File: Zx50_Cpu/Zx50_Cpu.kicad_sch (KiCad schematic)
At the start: 18 parts

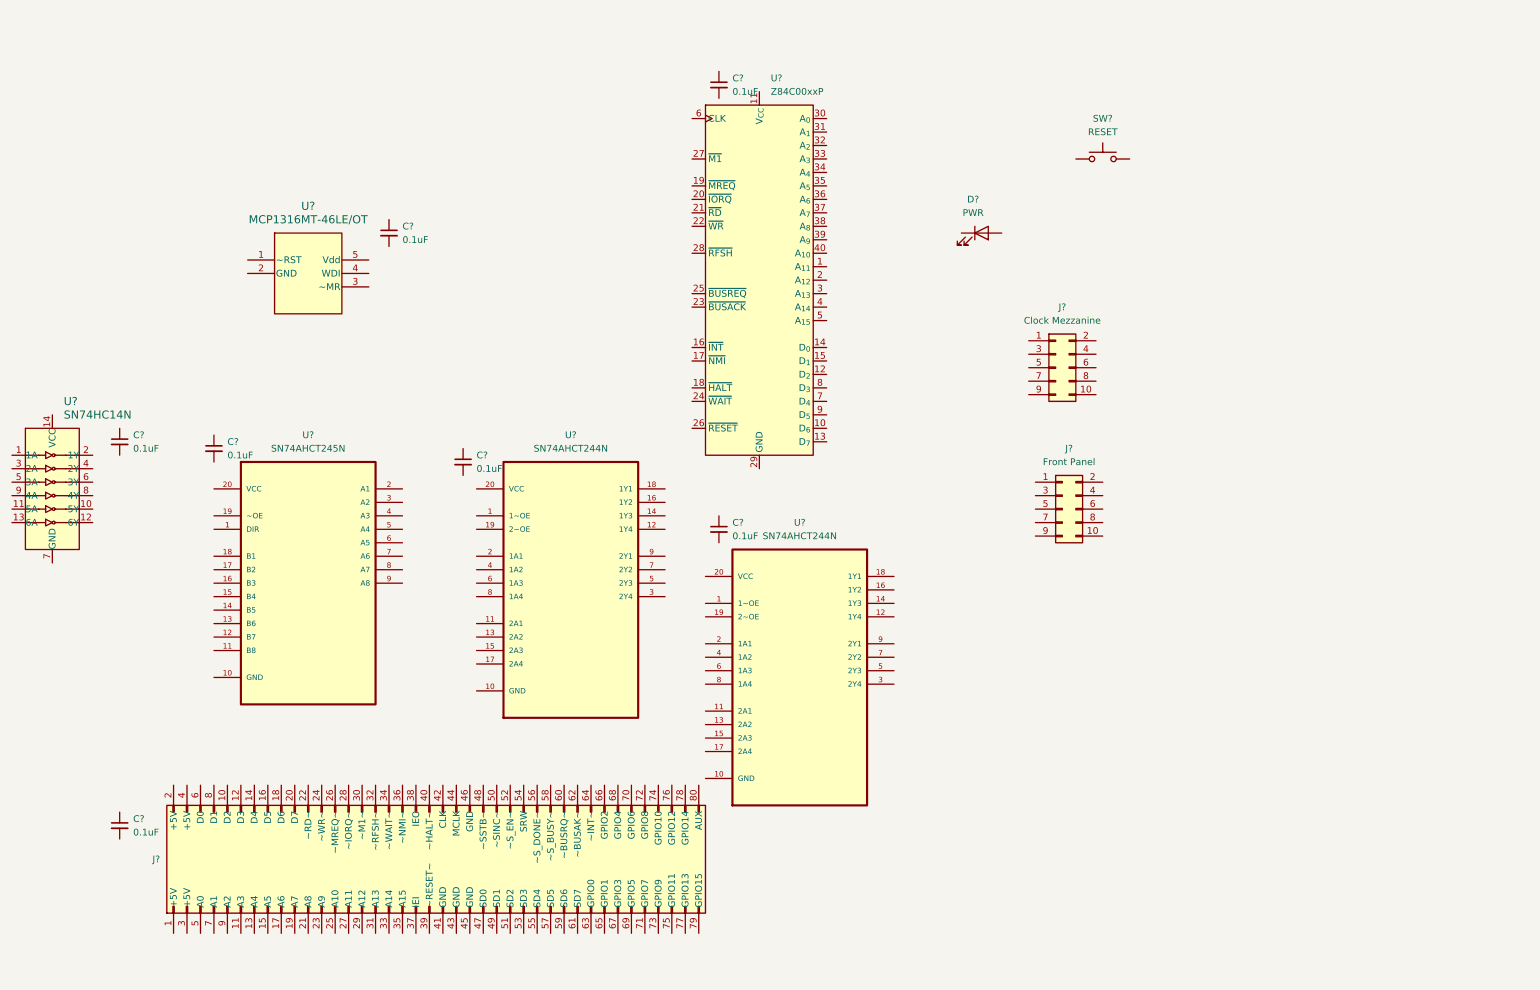
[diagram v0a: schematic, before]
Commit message: final cpu schematic before pcb layout
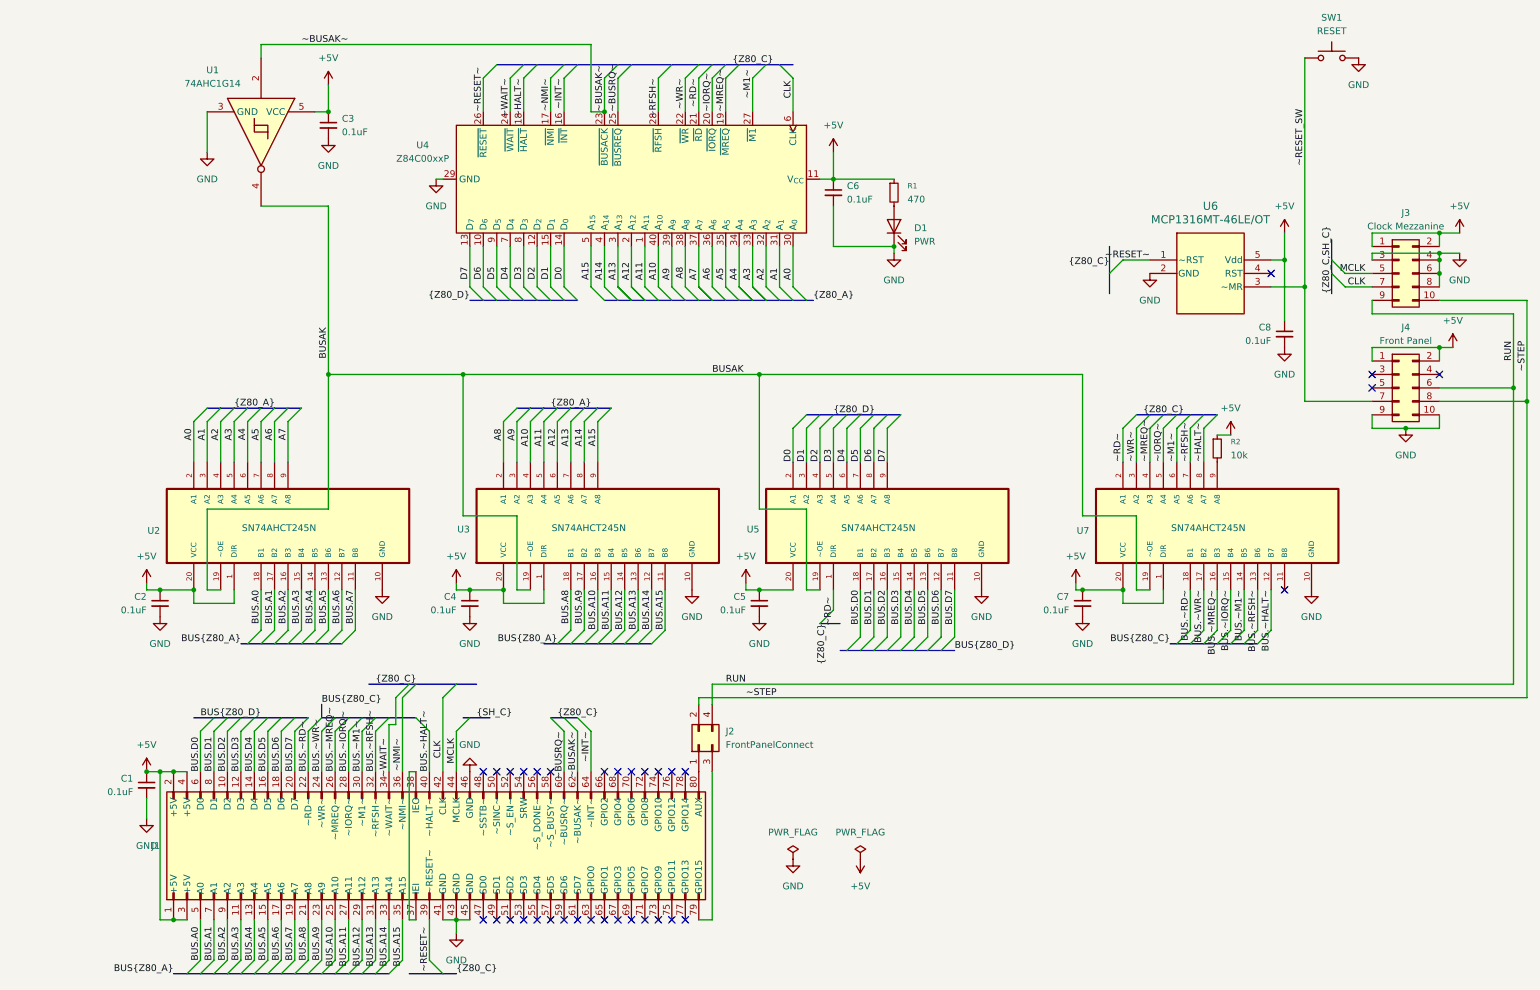
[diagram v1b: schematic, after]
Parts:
- removed C? (x4): 0.1uF, symbol zx50_symbols:C_0_1uF
- removed J?: Zx50_EdgeConnector, Connector_PinSocket_2.54mm:PinSocket_2x40_P2.54mm_Vertical_Oval, symbol zx50_symbols:Zx50_EdgeConnector
- removed U? (x2): SN74AHCT244N, Package_DIP:DIP-20_W7.62mm_Socket, symbol zx50_symbols:74AHCT244
- removed U?: SN74HC14N, digikey-footprints:DIP-14_W3mm, symbol dk_Logic-Gates-and-Inverters:SN74HC14N
- added C2, C3, C4, C7, C8: 0.1uF, Capacitor_THT:C_Disc_D5.0mm_W2.5mm_P5.00mm, symbol zx50_symbols:C_0_1uF
- added J1: Zx50_EdgeConnector, Connector_PinSocket_2.54mm:PinSocket_2x40_P2.54mm_Vertical_Oval, symbol zx50_symbols:Zx50_EdgeConnector
- added J2: FrontPanelConnect, Connector_PinSocket_2.54mm:PinSocket_2x02_P2.54mm_Vertical, symbol Connector_Generic:Conn_02x02_Odd_Even
- added R1: 470, Resistor_THT:R_Axial_DIN0207_L6.3mm_D2.5mm_P10.16mm_Horizontal, symbol Device:R_Small
- added R2: 10k, Resistor_THT:R_Axial_DIN0207_L6.3mm_D2.5mm_P10.16mm_Horizontal, symbol Device:R_Small
- added U1: 74AHC1G14, Package_TO_SOT_SMD:SOT-23-5_HandSoldering, symbol zx50_symbols:74AHC1G14
- added U2, U3, U7: SN74AHCT245N, Package_DIP:DIP-20_W7.62mm_Socket, symbol zx50_symbols:74AHCT245
- C1, C5, C6: renamed from C?; footprint (none) -> Capacitor_THT:C_Disc_D5.0mm_W2.5mm_P5.00mm; DigiKey_PN (none) -> BC1101CT-ND
- U5: renamed from U?; symbol zx50_symbols:SN74AHCT245N -> zx50_symbols:74AHCT245
- U6: renamed from U?; symbol zx50_symbols:MCP1316MT-46LE_OT -> zx50_symbols:MCP1318MT-46LE_OT; Digikey_PN MCP1316MT-46LE/OTCT-ND -> MCP1318MT-46LE/OTCT-ND
- gave numbers to parts that had none: 5
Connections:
- net ~RESET_SW: now reaches SW1.1
- net ~RESET_SW: now also J4.7 (Pin_7), U6.3 (~MR)
- net GND: now reaches SW1.2
- net GND: now also C1.2, C5.2, C6.2, D1.1 (K), J3.3 (Pin_3), J3.4 (Pin_4), J3.6 (Pin_6), J3.8 (Pin_8), J4.10 (Pin_10), J4.9 (Pin_9), U4.29 (GND), U5.10 (GND), U6.2 (GND), C2.2, C3.2, C4.2, C7.2, C8.2, J1.41 (GND), J1.43 (GND), J1.45 (GND), J1.46 (GND), U1.3 (GND), U2.10 (GND), U3.10 (GND), U7.10 (GND)
- net +5V: now reaches C5.1
- net +5V: now also C1.1, C6.1, J3.1 (Pin_1), J3.2 (Pin_2), J4.1 (Pin_1), J4.2 (Pin_2), U4.11 (V_{CC}), U5.20 (VCC), U6.5 (Vdd), C2.1, C3.1, C4.1, C7.1, C8.1, J1.1 (+5V), J1.2 (+5V), J1.3 (+5V), J1.4 (+5V), R1.1, R2.1, U1.5 (VCC), U2.1 (DIR), U2.20 (VCC), U3.1 (DIR), U3.20 (VCC), U7.1 (DIR), U7.20 (VCC)
- net ~RESET~: now reaches U6.1 (~RST)
- net ~RESET~: now also U4.26 (~{RESET}), J1.39 (~RESET~)
- net at D1.2 (A): now also R1.2
- net RUN: now reaches J4.6 (Pin_6)
- net RUN: now also J3.9 (Pin_9), J2.4 (Pin_4)
- net ~STEP: now reaches J4.8 (Pin_8)
- net ~STEP: now also J3.10 (Pin_10), J2.2 (Pin_2)
- net MCLK: now reaches J3.5 (Pin_5)
- net MCLK: now also J1.44 (MCLK)
- net CLK: now reaches J3.7 (Pin_7)
- net CLK: now also U4.6 (CLK), J1.42 (CLK)
- net A11: now reaches U4.1 (A_{11})
- net A11: now also U3.5 (A4)
- net D6: now reaches U4.10 (D_{6})
- net D6: now also U5.8 (A7)
- net D2: now reaches U4.12 (D_{2})
- net D2: now also U5.4 (A3)
- net D7: now reaches U4.13 (D_{7})
- net D7: now also U5.9 (A8)
- net D0: now reaches U4.14 (D_{0})
- net D0: now also U5.2 (A1)
- net D1: now reaches U4.15 (D_{1})
- net D1: now also U5.3 (A2)
- net ~INT~: now reaches U4.16 (~{INT})
- net ~INT~: now also J1.64 (~INT~)
- net ~NMI~: now reaches U4.17 (~{NMI})
- net ~NMI~: now also J1.36 (~NMI~)
- net ~HALT~: now reaches U4.18 (~{HALT})
- net ~HALT~: now also U7.8 (A7)
- net ~MREQ~: now reaches U4.19 (~{MREQ})
- net ~MREQ~: now also U7.4 (A3)
- net A12: now reaches U4.2 (A_{12})
- net A12: now also U3.6 (A5)
- net ~IORQ~: now reaches U4.20 (~{IORQ})
- net ~IORQ~: now also U7.5 (A4)
- net ~RD~: now reaches U4.21 (~{RD})
- net ~RD~: now also U5.1 (DIR), U7.2 (A1)
- net ~WR~: now reaches U4.22 (~{WR})
- net ~WR~: now also U7.3 (A2)
- net ~BUSAK~: now reaches U4.23 (~{BUSACK})
- net ~BUSAK~: now also J1.62 (~BUSAK~), U1.2
- net ~WAIT~: now reaches U4.24 (~{WAIT})
- net ~WAIT~: now also J1.34 (~WAIT~)
- net ~BUSRQ~: now reaches U4.25 (~{BUSREQ})
- net ~BUSRQ~: now also J1.60 (~BUSRQ~)
- net ~M1~: now reaches U4.27 (~{M1})
- net ~M1~: now also U7.6 (A5)
- net ~RFSH~: now reaches U4.28 (~{RFSH})
- net ~RFSH~: now also U7.7 (A6)
- net A13: now reaches U4.3 (A_{13})
- net A13: now also U3.7 (A6)
- net A0: now reaches U4.30 (A_{0})
- net A0: now also U2.2 (A1)
- net A1: now reaches U4.31 (A_{1})
- net A1: now also U2.3 (A2)
- net A2: now reaches U4.32 (A_{2})
- net A2: now also U2.4 (A3)
- net A3: now reaches U4.33 (A_{3})
- net A3: now also U2.5 (A4)
- net A4: now reaches U4.34 (A_{4})
- net A4: now also U2.6 (A5)
- net A5: now reaches U4.35 (A_{5})
- net A5: now also U2.7 (A6)
- net A6: now reaches U4.36 (A_{6})
- net A6: now also U2.8 (A7)
- net A7: now reaches U4.37 (A_{7})
- net A7: now also U2.9 (A8)
- net A8: now reaches U4.38 (A_{8})
- net A8: now also U3.2 (A1)
- net A9: now reaches U4.39 (A_{9})
- net A9: now also U3.3 (A2)
- net A14: now reaches U4.4 (A_{14})
- net A14: now also U3.8 (A7)
- net A10: now reaches U4.40 (A_{10})
- net A10: now also U3.4 (A3)
- net A15: now reaches U4.5 (A_{15})
- net A15: now also U3.9 (A8)
- net D4: now reaches U4.7 (D_{4})
- net D4: now also U5.6 (A5)
- net D3: now reaches U4.8 (D_{3})
- net D3: now also U5.5 (A4)
- net D5: now reaches U4.9 (D_{5})
- net D5: now also U5.7 (A6)
- net BUS.D7: now reaches U5.11 (B8)
- net BUS.D7: now also J1.20 (D7)
- net BUS.D6: now reaches U5.12 (B7)
- net BUS.D6: now also J1.18 (D6)
- net BUS.D5: now reaches U5.13 (B6)
- net BUS.D5: now also J1.16 (D5)
- net BUS.D4: now reaches U5.14 (B5)
- net BUS.D4: now also J1.14 (D4)
- net BUS.D3: now reaches U5.15 (B4)
- net BUS.D3: now also J1.12 (D3)
- net BUS.D2: now reaches U5.16 (B3)
- net BUS.D2: now also J1.10 (D2)
- net BUS.D1: now reaches U5.17 (B2)
- net BUS.D1: now also J1.8 (D1)
- net BUS.D0: now reaches U5.18 (B1)
- net BUS.D0: now also J1.6 (D0)
- net BUSAK: now reaches U5.19 (~OE)
- net BUSAK: now also U1.4, U2.19 (~OE), U3.19 (~OE), U7.19 (~OE)
- new net: R2.2, U7.9 (A8)
- new net: J1.37 (IEI), J1.38 (IEO)
- new net: J1.79 (GPIO15), J2.3 (Pin_3)
- new net: J1.80 (AUX), J2.1 (Pin_1)
- new net BUS.A0: J1.5 (A0), U2.18 (B1)
- new net BUS.A1: J1.7 (A1), U2.17 (B2)
- new net BUS.A10: J1.25 (A10), U3.16 (B3)
- new net BUS.A11: J1.27 (A11), U3.15 (B4)
- new net BUS.A12: J1.29 (A12), U3.14 (B5)
- new net BUS.A13: J1.31 (A13), U3.13 (B6)
- new net BUS.A14: J1.33 (A14), U3.12 (B7)
- new net BUS.A15: J1.35 (A15), U3.11 (B8)
- new net BUS.A2: J1.9 (A2), U2.16 (B3)
- new net BUS.A3: J1.11 (A3), U2.15 (B4)
- new net BUS.A4: J1.13 (A4), U2.14 (B5)
- new net BUS.A5: J1.15 (A5), U2.13 (B6)
- new net BUS.A6: J1.17 (A6), U2.12 (B7)
- new net BUS.A7: J1.19 (A7), U2.11 (B8)
- new net BUS.A8: J1.21 (A8), U3.18 (B1)
- new net BUS.A9: J1.23 (A9), U3.17 (B2)
- new net BUS.~HALT~: J1.40 (~HALT~), U7.12 (B7)
- new net BUS.~IORQ~: J1.28 (~IORQ~), U7.15 (B4)
- new net BUS.~M1~: J1.30 (~M1~), U7.14 (B5)
- new net BUS.~MREQ~: J1.26 (~MREQ~), U7.16 (B3)
- new net BUS.~RD~: J1.22 (~RD~), U7.18 (B1)
- new net BUS.~RFSH~: J1.32 (~RFSH~), U7.13 (B6)
- new net BUS.~WR~: J1.24 (~WR~), U7.17 (B2)
- no-connect marks 0 -> 34
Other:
- moved on the sheet: C1, C5, C6, D1, J3, J4, SW1, U4, U5, U6
